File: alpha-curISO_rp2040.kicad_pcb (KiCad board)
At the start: 2 copper layers, 248.6 x 81.9 mm, 195 parts, among them J1 SWD, J2 USB_C_Receptacle_USB2.0, SW1 SW_Push_45deg, SW10 SW_Push_45deg, SW11 SW_Push_45deg, SW12 SW_Push_45deg, SW12(2)1 SW_Push_45deg, SW13 SW_Push_45deg, SW14 SW_Push_45deg, SW15 SW_Push_45deg, SW16 SW_Push_45deg, SW17 SW_Push_45deg, SW18 SW_Push_45deg, SW19 SW_Push_45deg, SW2 SW_Push_45deg, SW20 SW_Push_45deg, SW21 SW_Push_45deg, SW22 SW_Push_45deg, SW23 SW_Push_45deg, SW24 SW_Push_45deg, SW24(1.5)1 SW_Push_45deg, SW25 SW_Push_45deg, SW25(1.5)1 SW_Push_45deg, SW26 SW_Push_45deg, SW26(2)1 SW_Push_45deg, SW26(ISO)1 SW_Push_45deg, SW27 SW_Push, SW27(1.25)1 SW_Push_45deg, SW27(1.5)1 SW_Push_45deg, SW27(ortho)1 SW_Push_45deg, SW28 SW_Push_45deg, SW28(1.5stagger)1 SW_Push_45deg, SW28(ortho)1 SW_Push_45deg, SW29 SW_Push_45deg, SW29(1.5stagger)1 SW_Push_45deg, SW29(ortho)1 SW_Push_45deg, SW3 SW_Push_45deg, SW30 SW_Push_45deg, SW30(1.5stagger)1 SW_Push_45deg, SW30(ortho)1 SW_Push_45deg, SW31 SW_Push_45deg, SW31(1.5stagger)1 SW_Push_45deg, SW31(ortho)1 SW_Push_45deg, SW32 SW_Push_45deg, SW32(1.5stagger)1 SW_Push_45deg, SW32(ortho)1 SW_Push_45deg, SW33 SW_Push_45deg, SW33(1.5stagger)1 SW_Push_45deg, SW33(ortho)1 SW_Push_45deg, SW34 SW_Push_45deg, SW34(1.5stagger)1 SW_Push_45deg, SW34(ortho)1 SW_Push_45deg, SW35 SW_Push_45deg, SW35(1.5stagger)1 SW_Push_45deg, SW35(ortho)1 SW_Push_45deg, SW36 SW_Push_45deg, SW36(1.5stagger)1 SW_Push_45deg, SW36(ortho)1 SW_Push_45deg, SW37 SW_Push_45deg, SW37(1.5stagger)1 SW_Push_45deg, SW37(ortho)1 SW_Push_45deg, SW38(1.25)1 SW_Push_45deg, SW38(1.5)1 SW_Push_45deg, SW38(ortho)1 SW_Push_45deg, SW39 SW_Push_45deg, SW39(1.5)1 SW_Push_45deg, SW4 SW_Push_45deg, SW40 SW_Push_45deg, SW40(3)1 SW_Push_45deg, SW41 SW_Push_45deg, SW41(1.5)1 SW_Push_45deg, SW42(1.25)1 SW_Push_45deg, SW42(1.5)1 SW_Push_45deg, SW42(3)1 SW_Push_45deg, SW43(1.75)1 SW_Push_45deg, SW43(2)1 SW_Push_45deg, SW44(3)1 SW_Push_45deg, SW44(6)1 SW_Push_45deg, SW45(1.75)1 SW_Push_45deg, SW45(2)1 SW_Push_45deg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

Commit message: MCU routing, RGB leds
MCU first routing draft finished

added RGB leds instead of diodes
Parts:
- added LED1: YS-SK6812MINI-E, Keebio-Parts:SK6812-MINI-E, B.Cu at (144.5, 101.6)
- added LED2: YS-SK6812MINI-E, Keebio-Parts:SK6812-MINI-E, B.Cu at (147.6, 96.8)
- added LED3: YS-SK6812MINI-E, Keebio-Parts:SK6812-MINI-E, B.Cu at (150.8, 101.6)
- added SW44(4)1: SW_Push_45deg, CherryMX_4.00u:CherryMX_4.00u, F.Cu at (147.6, 120.7)
- moved R9 119.2 mm to (37.3, 157.2)
- moved R10 119.2 mm to (43.7, 157.2)
- moved R8 119.2 mm to (40.5, 152.4)
- moved D51 105.5 mm to (54.7, 157.2)
- moved D52 105.5 mm to (61.1, 157.2)
- moved D50 105.5 mm to (57.9, 152.4)
- moved J1 11.4 mm to (25.4, 108.0), turned to 180 degrees
- moved R3 9.65 mm to (27.9, 108.6), turned to 90 degrees
- moved C5 8.30 mm to (38.7, 72.4), turned to 0 degrees
- moved C6 7.73 mm to (38.7, 73.4), turned to 0 degrees
- moved U3 3.86 mm to (39.2, 69.6), turned to 90 degrees
- moved C2 2.79 mm to (51.9, 101.5)
- moved C1 2.52 mm to (46.0, 101.3)
- moved Y1 2.52 mm to (48.8, 101.6)
- moved C17 1.26 mm to (51.8, 82.5), turned to 0 degrees
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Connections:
- net R_col3 renamed COL6
- net R_row6 renamed COL8
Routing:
- net +3V3: track 0.00 -> 108.2 mm, vias 0 -> 4
- net GND: track 0.00 -> 70.3 mm, vias 0 -> 15
- net SWCLK: track 0.00 -> 49.8 mm
- net SWD: track 0.00 -> 46.6 mm
- net CS: track 0.00 -> 39.7 mm
- net RESET: track 0.00 -> 39.4 mm
- net SD1: track 0.00 -> 33.6 mm
- net SD3: track 0.00 -> 29.0 mm
- net SD2: track 0.00 -> 28.8 mm
- net QSPI_CLK: track 0.00 -> 27.3 mm
- net +1V1: track 0.00 -> 27.0 mm, vias 0 -> 4
- net SD0: track 0.00 -> 25.8 mm
- net XTAL_IN: track 0.00 -> 18.1 mm
- net ROW1: track 216.6 -> 200.4 mm
- net VBUS: track 0.00 -> 14.6 mm
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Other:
- board text added: "rotary needs to be flipped sidewards for the oled to have space"
- board text removed: "still need to add 4u footprint sszczep-switch-libraries has some, but think those come without stabs and need to be edited accordingly"

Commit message: changed MCU placement, redid routing
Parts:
- removed SW25(1.5)1: SW_Push_45deg, MX_Only:MXOnly-1.5U-NoLED
- moved J1 117.0 mm to (137.6, 74.6), turned to 0 degrees
- moved R3 112.6 mm to (134.9, 73.4), turned to -90 degrees
- moved C1 77.3 mm to (115.7, 67.8), turned to -135 degrees
- moved Y1 74.1 mm to (113.7, 65.8), turned to 135 degrees
- moved C2 73.7 mm to (115.4, 64.1), turned to 135 degrees
- moved R7 71.3 mm to (112.0, 67.4), turned to 135 degrees
- moved C14 69.3 mm to (109.5, 67.9), turned to 0 degrees
- moved C9 68.8 mm to (109.5, 66.8), turned to 0 degrees
- moved C11 64.9 mm to (102.6, 73.7), turned to -90 degrees
- moved U1 58.7 mm to (101.6, 66.7), turned to -90 degrees
- moved C8 58.5 mm to (97.5, 73.1), turned to -90 degrees
- moved C16 57.1 mm to (96.3, 73.1), turned to -90 degrees
- moved C13 56.5 mm to (102.6, 59.6), turned to 90 degrees
- moved C7 54.2 mm to (95.5, 70.7), turned to 180 degrees
- moved C10 53.4 mm to (95.5, 69.7), turned to 180 degrees
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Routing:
- net D_N: track 8.97 -> 50.8 mm
- net D_P: track 8.81 -> 50.1 mm
- net +3V3: track 108.2 -> 130.6 mm, vias 4 -> 5
- net COL4: track 119.1 -> 100.1 mm
- net ROW0: track 208.7 -> 193.0 mm
- net SWCLK: track 49.8 -> 35.7 mm
- net SD3: track 29.0 -> 20.3 mm
- net QSPI_CLK: track 27.3 -> 20.8 mm
- net XTAL_IN: track 18.1 -> 11.7 mm
- net SWD: track 46.6 -> 40.6 mm
- net SD0: track 25.8 -> 20.8 mm
- net /rp2040 components/XTAL_O: track 8.04 -> 3.66 mm
- net /rp2040 components/USB_BOOT: track 11.2 -> 8.01 mm
- net RESET: track 39.4 -> 36.4 mm
- net GND: track 70.3 -> 67.4 mm, vias 15 -> 14
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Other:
- board text removed: "ISO stabs collide"

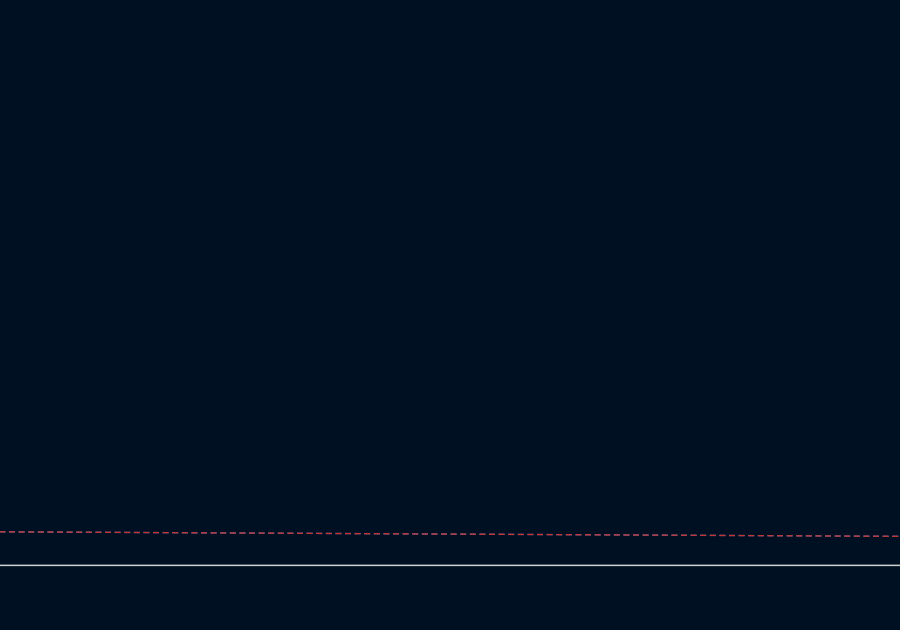
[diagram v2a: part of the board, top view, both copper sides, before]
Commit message: added underglow to schematics
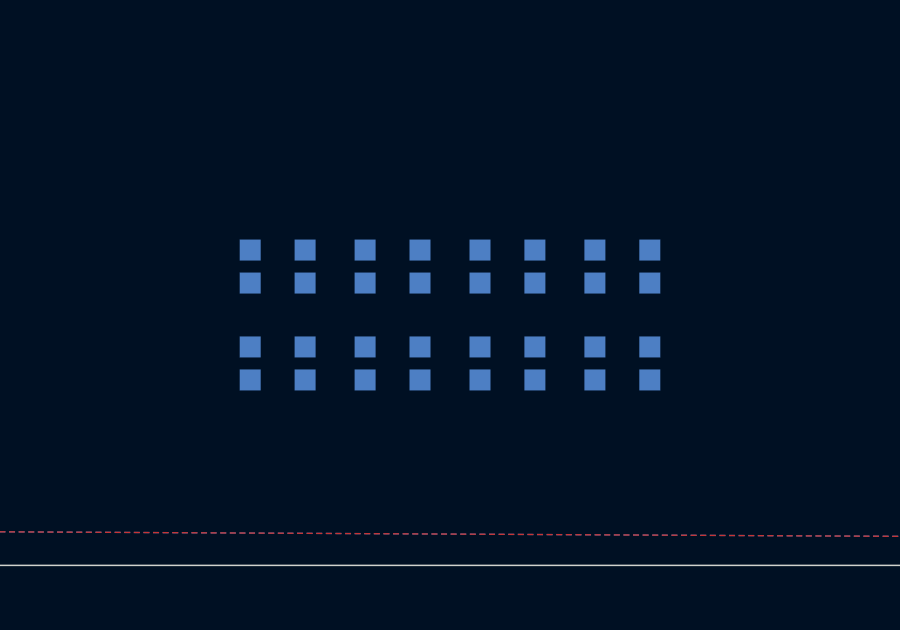
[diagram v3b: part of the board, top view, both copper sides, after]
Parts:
- added LED10: YS-SK6812MINI-E, CrumpPrints:WS2812-2020, B.Cu at (161.0, 42.4)
- added LED11: YS-SK6812MINI-E, CrumpPrints:WS2812-2020, B.Cu at (161.0, 39.2)
- added LED4: YS-SK6812MINI-E, CrumpPrints:WS2812-2020, B.Cu at (172.5, 42.4)
- added LED5: YS-SK6812MINI-E, CrumpPrints:WS2812-2020, B.Cu at (172.5, 39.2)
- added LED6: YS-SK6812MINI-E, CrumpPrints:WS2812-2020, B.Cu at (168.7, 42.4)
- added LED7: YS-SK6812MINI-E, CrumpPrints:WS2812-2020, B.Cu at (164.9, 39.2)
- added LED8: YS-SK6812MINI-E, CrumpPrints:WS2812-2020, B.Cu at (164.9, 42.4)
- added LED9: YS-SK6812MINI-E, CrumpPrints:WS2812-2020, B.Cu at (168.7, 39.2)
